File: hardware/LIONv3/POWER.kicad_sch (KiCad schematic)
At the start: 24 parts, among them U10 INA226AIDGSR, U11 TPS259474ARPWR, U12 XL-1608UGC-04, U13 XL-1608SURC-06, U20 TLV76733DRVR

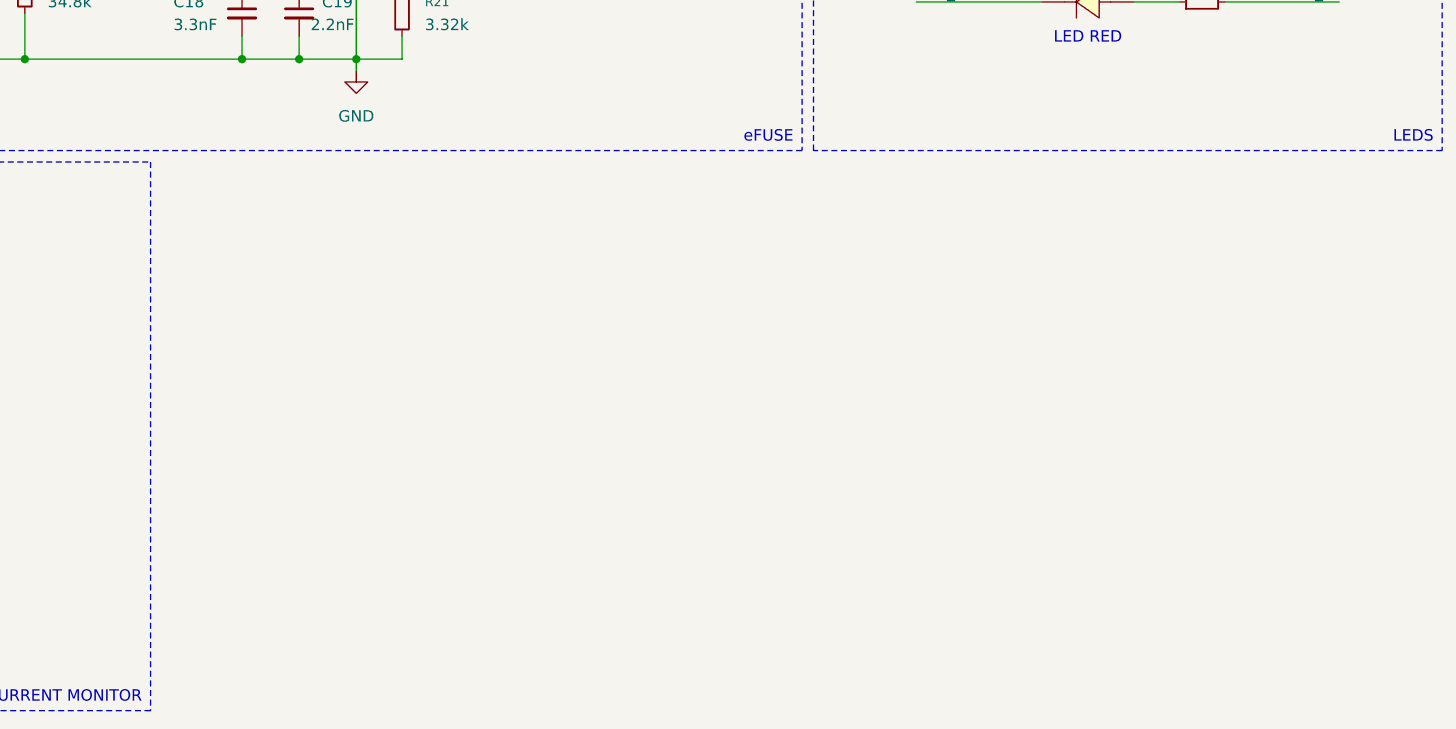
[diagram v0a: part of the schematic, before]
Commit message: feat(hardware): add power layout
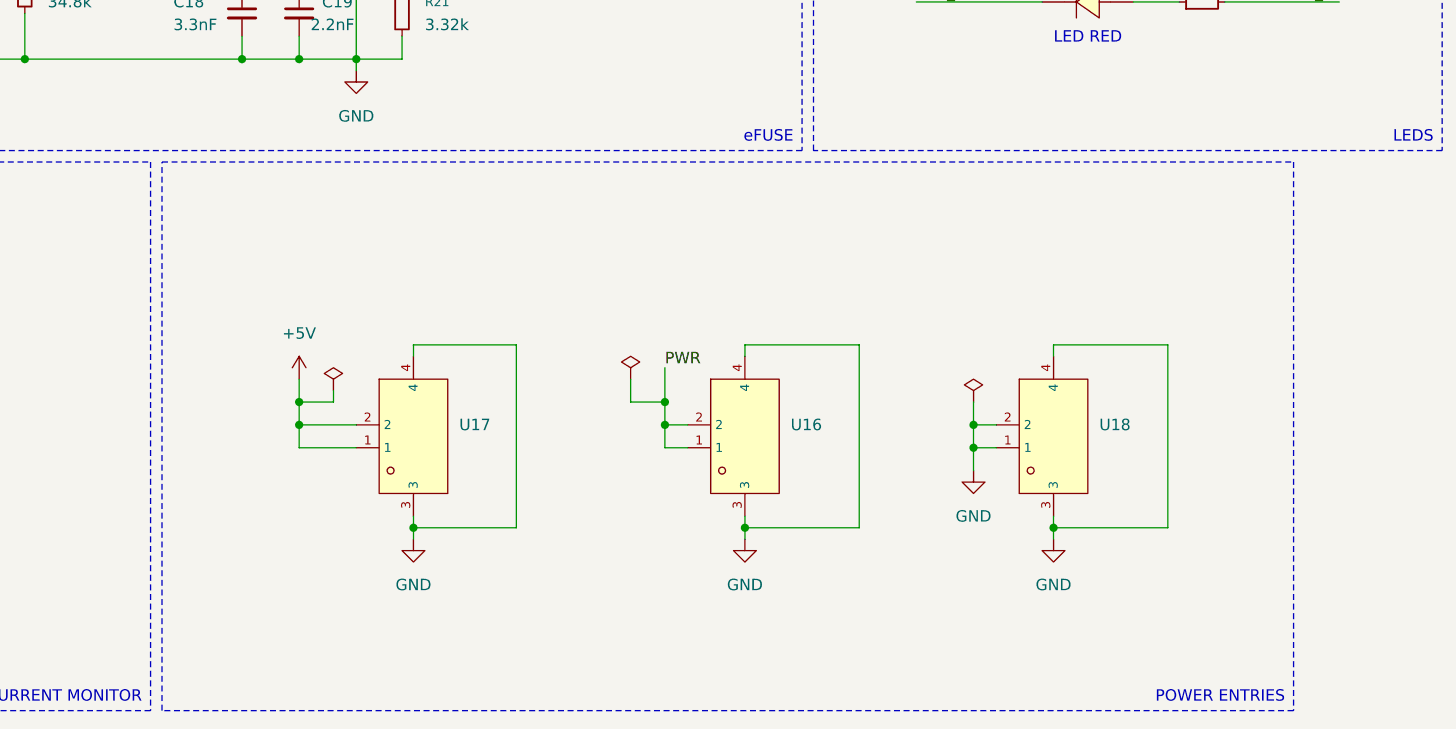
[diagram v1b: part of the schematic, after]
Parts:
- added U16, U17, U18: HC-1_25-2PWT, LIONv3-Footprints:CONN-SMD_2P-P1.25-HC-1.25-2PWT, symbol LIONv3-Symbols:HC-1_25-2PWT
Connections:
- net +5V: now also U17.1, U17.2
- net GND: now also U16.3, U16.4, U17.3, U17.4, U18.1, U18.2, U18.3, U18.4
- net PWR: now also U16.1, U16.2

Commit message: Add TVS diode protection (ESD9B3.3ST5G)
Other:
- note added: "AUTO-RETRY VERSION (110ms)"
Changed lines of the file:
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@@
+		)
+	)
+	(text "AUTO-RETRY VERSION (110ms)"
+		(exclude_from_sim no)
+		(at 194.31 55.88 0)
+		(effects
+			(font
+				(size 1.27 1.27)
+			)
 		)
 	)

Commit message: feat(hardware): Add TVS diode protection on USB lines (USBLC6-2SC6)
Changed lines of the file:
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@@
-	)
-	(junction
-		(at 196.85 97.79)
-		(diameter 0)
-		(color 0 0 0 0)
 	)
 	(junction
@@
 	(wire
 		(pts
-			(xy 193.04 95.25) (xy 193.04 97.79)
-		)
-		(stroke
-			(width 0)
-			(type default)
-		)
-	)
-	(wire
-		(pts
 			(xy 162.56 49.53) (xy 162.56 59.69)
 		)
@@
 	(wire
 		(pts
-			(xy 196.85 100.33) (xy 196.85 97.79)
+			(xy 196.85 93.98) (xy 196.85 100.33)
 		)
 		(stroke
@@
 	(wire
 		(pts
-			(xy 193.04 97.79) (xy 196.85 97.79)
-		)
-		(stroke
-			(width 0)
-			(type default)
-		)
-	)
-	(wire
-		(pts
 			(xy 149.86 59.69) (xy 149.86 57.15)
 		)
@@
 		(pts
 			(xy 104.14 107.95) (xy 104.14 106.68)
-		)
-		(stroke
-			(width 0)
-			(type default)
-		)
-	)
-	(wire
-		(pts
-			(xy 196.85 93.98) (xy 196.85 97.79)
 		)
 		(stroke
@@
 					(unit 1)
 				)
-			)
-		)
-	)
-	(symbol
-		(lib_id "power:PWR_FLAG")
-		(at 193.04 95.25 0)
-		(unit 1)
-		(body_style 1)
-		(exclude_from_sim no)
-		(in_bom yes)
-		(on_board yes)
-		(in_pos_files yes)
-		(dnp no)
-		(fields_autoplaced yes)
-		(property "Reference" "#FLG09"
-			(at 193.04 93.345 0)
-			(hide yes)
-			(show_name no)
-			(do_not_autoplace no)
-			(effects
-				(font
-					(size 1.27 1.27)
-				)
-			)
-		)
-		(property "Value" "PWR_FLAG"
-			(at 193.04 90.17 0)
-			(hide yes)
-			(show_name no)
-			(do_not_autoplace no)
-			(effects
-				(font
-					(size 1.27 1.27)
-				)
-			)
-		)
-		(property "Footprint" ""
-			(at 193.04 95.25 0)
-			(hide yes)
-			(show_name no)
-			(do_not_autoplace no)
-			(effects
-				(font
-					(size 1.27 1.27)
-				)
-			)
-		)
-		(property "Datasheet" ""
-			(at 193.04 95.25 0)
-			(hide yes)
-			(show_name no)
-			(do_not_autoplace no)
-			(effects
-				(font
-					(size 1.27 1.27)
-				)
-			)
-		)
-		(property "Description" "Special symbol for telling ERC where power comes from"
-			(at 193.04 95.25 0)
-			(hide yes)
-			(show_name no)
-			(do_not_autoplace no)
-			(effects
-				(font
-					(size 1.27 1.27)
-				)
-			)
-		)
-		(pin "1"
-		)
-		(instances
-			(project "LIONv3"
-				(path "/3cc9e06f-00d0-4bec-822f-2e156022ced4/78bf7d09-3355-4da6-a4af-8df1bf47cdde"
-					(reference "#FLG09")
-					(unit 1)
-				)

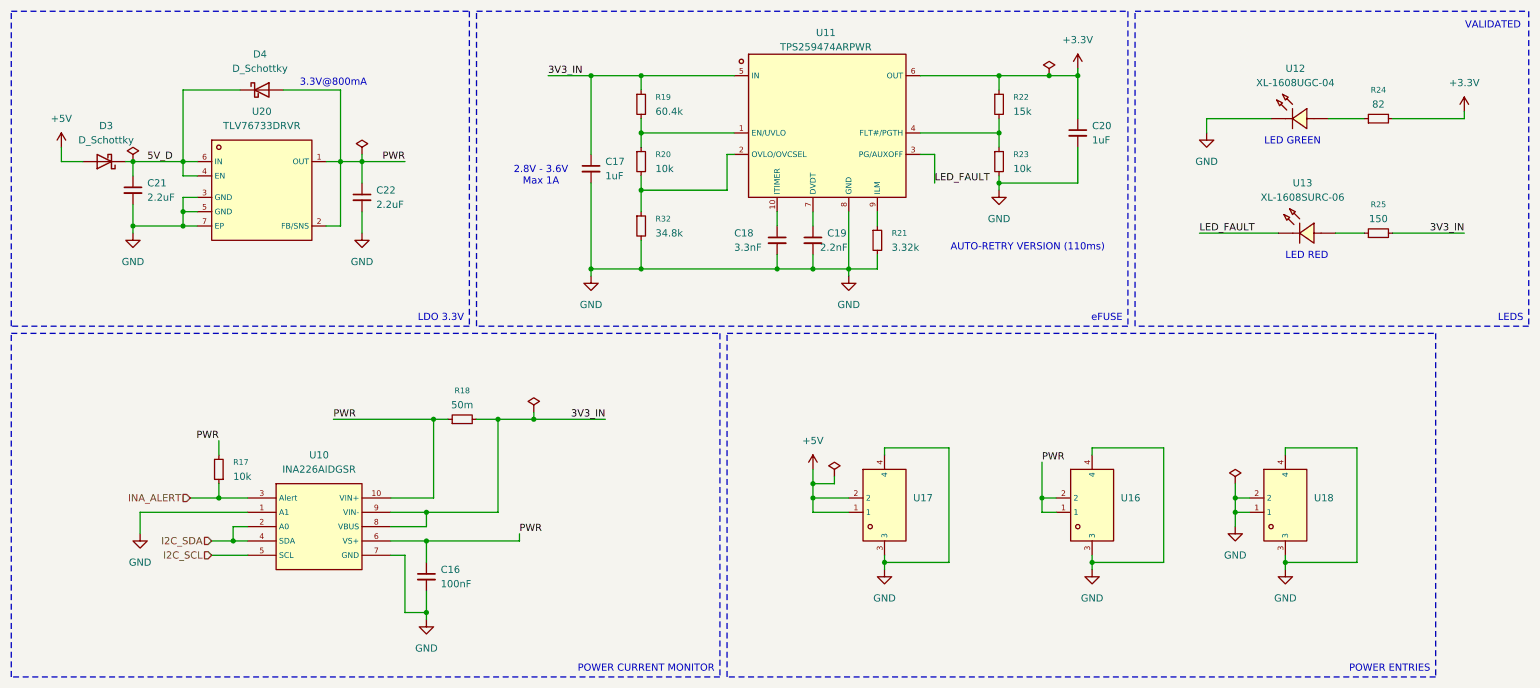
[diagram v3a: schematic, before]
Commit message: feat(hardware): Add ORing (USB VBUS back-feed)
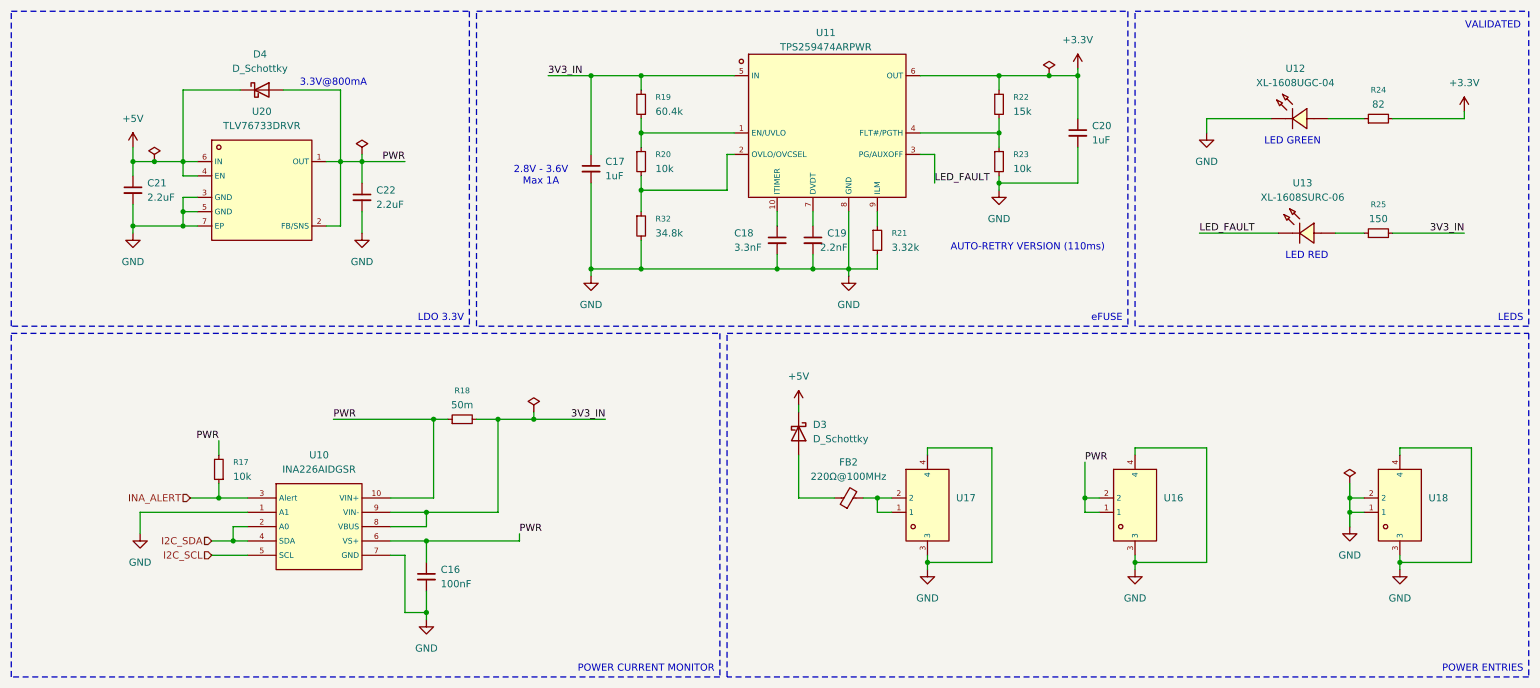
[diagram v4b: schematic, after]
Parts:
- added FB2: 220Ω@100MHz, Capacitor_SMD:C_0805_2012Metric, symbol Device:FerriteBead_Small
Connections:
- net 5V_D is gone; now on net +5V: C21.1, D3.1 (K), D4.1 (K), U20.4 (EN), U20.6 (IN)
- net +5V: no longer D3.2 (A), U17.1, U17.2
- new net: D3.2 (A), FB2.1
- new net: FB2.2, U17.1, U17.2
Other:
- moved on the sheet: U16, U17, U18

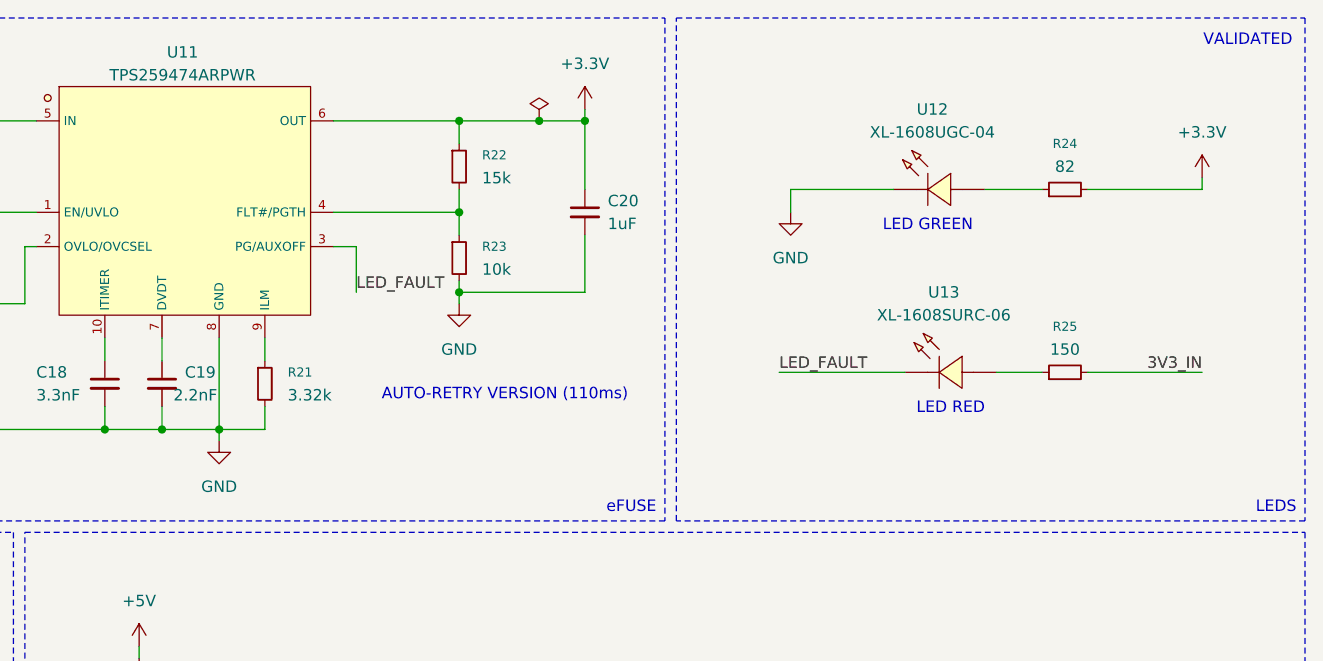
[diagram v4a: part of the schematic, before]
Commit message: feat(hardware): improves LED series currents
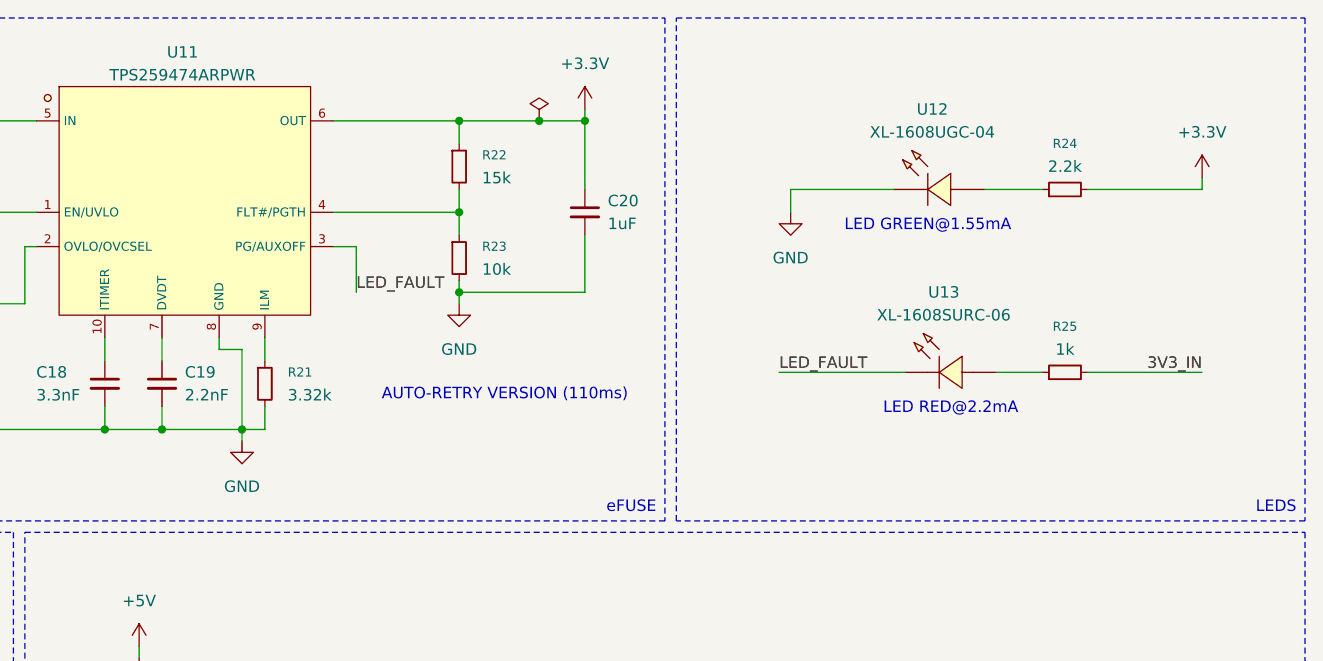
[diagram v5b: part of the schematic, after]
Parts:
- R24: value 82 -> 2.2k
- R25: value 150 -> 1k
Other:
- note added: "LED GREEN@1.55mA"
- note added: "LED RED@2.2mA"
- note removed: "LED GREEN"
- note removed: "LED RED"
- note removed: "VALIDATED"
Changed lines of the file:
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@@
 		)
 	)
-	(text "VALIDATED"
-		(exclude_from_sim no)
-		(at 276.86 16.51 0)
-		(effects
-			(font
-				(size 1.27 1.27)
-			)
-		)
-	)
 	(text "AUTO-RETRY VERSION (110ms)"
 		(exclude_from_sim no)
@@
 		)
 	)
-	(text "LED GREEN"
+	(text "LED GREEN@1.55mA"
 		(exclude_from_sim no)
 		(at 241.3 37.084 0)
@@
 		)
 	)
-	(text "LED RED"
+	(text "LED RED@2.2mA"
 		(exclude_from_sim no)
 		(at 243.84 57.404 0)
@@
 	)
 	(junction
+		(at 165.1 59.69)
+		(diameter 0)
+		(color 0 0 0 0)
+	)
+	(junction
 		(at 100.33 86.36)
 		(diameter 0)
@@
 	)
 	(junction
-		(at 162.56 59.69)
-		(diameter 0)
-		(color 0 0 0 0)
-	)
-	(junction
 		(at 156.21 59.69)
 		(diameter 0)
@@
 	(wire
 		(pts
-			(xy 156.21 59.69) (xy 162.56 59.69)
+			(xy 156.21 59.69) (xy 167.64 59.69)
 		)
 		(stroke
@@
 	(wire
 		(pts
-			(xy 162.56 59.69) (xy 162.56 60.96)
+			(xy 165.1 59.69) (xy 165.1 60.96)
 		)
 		(stroke
@@
 	(wire
 		(pts
+			(xy 165.1 50.8) (xy 162.56 50.8)
+		)
+		(stroke
+			(width 0)
+			(type default)
+		)
+	)
+	(wire
+		(pts
 			(xy 116.84 59.69) (xy 125.73 59.69)
 		)
@@
 	(wire
 		(pts
-			(xy 167.64 59.69) (xy 162.56 59.69)
-		)
-		(stroke
-			(width 0)
-			(type default)
-		)
-	)
-	(wire
-		(pts
 			(xy 177.8 39.37) (xy 177.8 44.45)
 		)
@@
 	(wire
 		(pts
-			(xy 162.56 49.53) (xy 162.56 59.69)
+			(xy 165.1 50.8) (xy 165.1 59.69)
 		)
 		(stroke
@@
 	(wire
 		(pts
+			(xy 162.56 50.8) (xy 162.56 49.53)
+		)
+		(stroke
+			(width 0)
+			(type default)
+		)
+	)
+	(wire
+		(pts
 			(xy 156.21 59.69) (xy 156.21 57.15)
 		)
@@
 		(dnp no)
 		(property "Reference" "C19"
-			(at 158.75 53.3462 0)
+			(at 158.75 53.34 0)
 			(show_name no)
 			(do_not_autoplace no)
@@
 		)
 		(property "Value" "2.2nF"
-			(at 157.48 55.88 0)
+			(at 158.75 55.8738 0)
 			(show_name no)
 			(do_not_autoplace no)
@@
 	(symbol
 		(lib_id "power:GND")
-		(at 162.56 60.96 0)
+		(at 165.1 60.96 0)
 		(unit 1)
 		(body_style 1)
@@
 		(fields_autoplaced yes)
 		(property "Reference" "#PWR040"
-			(at 162.56 67.31 0)
+			(at 165.1 67.31 0)
 			(hide yes)
 			(show_name no)
@@
 		)
 		(property "Value" "GND"
-			(at 162.56 66.04 0)
+			(at 165.1 66.04 0)
 			(show_name no)
 			(do_not_autoplace no)
@@
 		)
 		(property "Footprint" ""
-			(at 162.56 60.96 0)
+			(at 165.1 60.96 0)
 			(hide yes)
 			(show_name no)
@@
 		)
 		(property "Datasheet" ""
-			(at 162.56 60.96 0)
+			(at 165.1 60.96 0)
 			(hide yes)
 			(show_name no)
@@
 		)
 		(property "Description" "Power symbol creates a global label with name \"GND\" , ground"
-			(at 162.56 60.96 0)
+			(at 165.1 60.96 0)
 			(hide yes)
 			(show_name no)
@@
 			)
 		)
-		(property "Value" "82"
+		(property "Value" "2.2k"
 			(at 256.54 30.48 90)
 			(show_name no)
@@
 			)
 		)
-		(property "Datasheet" "https://atta.szlcsc.com/upload/public/pdf/source/20190115/C264450_D840E7E570138F41CCE67133F241C738.pdf"
+		(property "Datasheet" "https://www.lcsc.com/datasheet/C965804.pdf"
 			(at 240.284 32.893 0)
 			(hide yes)
@@
 			)
 		)
-		(property "Value" "150"
+		(property "Value" "1k"
 			(at 256.54 50.8 90)
 			(show_name no)
@@
 			)
 		)
-		(property "Datasheet" "https://item.szlcsc.com/221679.html"
+		(property "Datasheet" "https://www.lcsc.com/datasheet/C965799.pdf"
 			(at 241.554 53.213 0)
 			(hide yes)

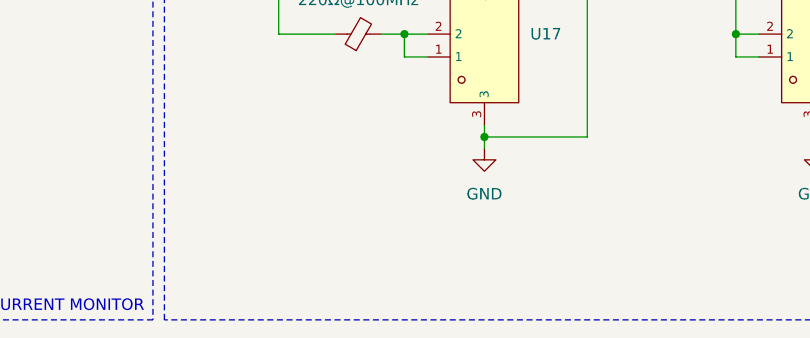
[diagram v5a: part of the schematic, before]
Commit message: feat(hardware): removes R1 and C3 from reset switch
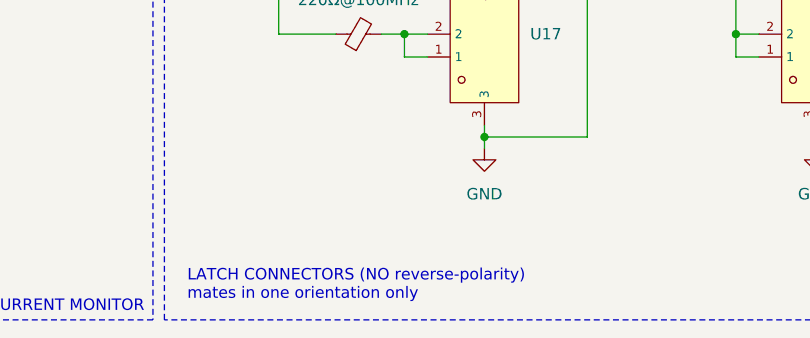
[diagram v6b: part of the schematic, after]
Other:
- note added: "LATCH CONNECTORS (NO reverse-polarity) mates in one orientation only"
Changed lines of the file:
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@@
 		)
 	)
+	(text "LATCH CONNECTORS (NO reverse-polarity)\nmates in one orientation only"
+		(exclude_from_sim no)
+		(at 143.51 128.27 0)
+		(effects
+			(font
+				(size 1.27 1.27)
+			)
+			(justify left)
+		)
+	)
 	(text_box "POWER CURRENT MONITOR"
 		(exclude_from_sim no)
@@
 			)
 		)
-		(property "Datasheet" "https://www.lcsc.com/datasheet/C2848334.pdf"
+		(property "Datasheet" "https://www.ti.com/lit/ds/symlink/tlv767.pdf"
 			(at 57.404 44.323 0)
 			(hide yes)
@@
 			)
 		)
-		(property "Datasheet" "https://atta.szlcsc.com/upload/public/pdf/source/20210728/C2845379_48B7DC28A4B35DB030A7253F7C3FD974.pdf"
+		(property "Datasheet" "https://www.lcsc.com/datasheet/C2845379.pdf"
 			(at 256.794 101.473 0)
 			(hide yes)
@@
 			)
 		)
-		(property "Datasheet" "https://atta.szlcsc.com/upload/public/pdf/source/20210728/C2845379_48B7DC28A4B35DB030A7253F7C3FD974.pdf"
+		(property "Datasheet" "https://www.lcsc.com/datasheet/C2845379.pdf"
 			(at 209.804 101.473 0)
 			(hide yes)
@@
 			)
 		)
-		(property "Datasheet" "https://atta.szlcsc.com/upload/public/pdf/source/20210728/C2845379_48B7DC28A4B35DB030A7253F7C3FD974.pdf"
+		(property "Datasheet" "https://www.lcsc.com/datasheet/C2845379.pdf"
 			(at 172.974 101.473 0)
 			(hide yes)
